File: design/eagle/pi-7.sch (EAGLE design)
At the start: 13 parts

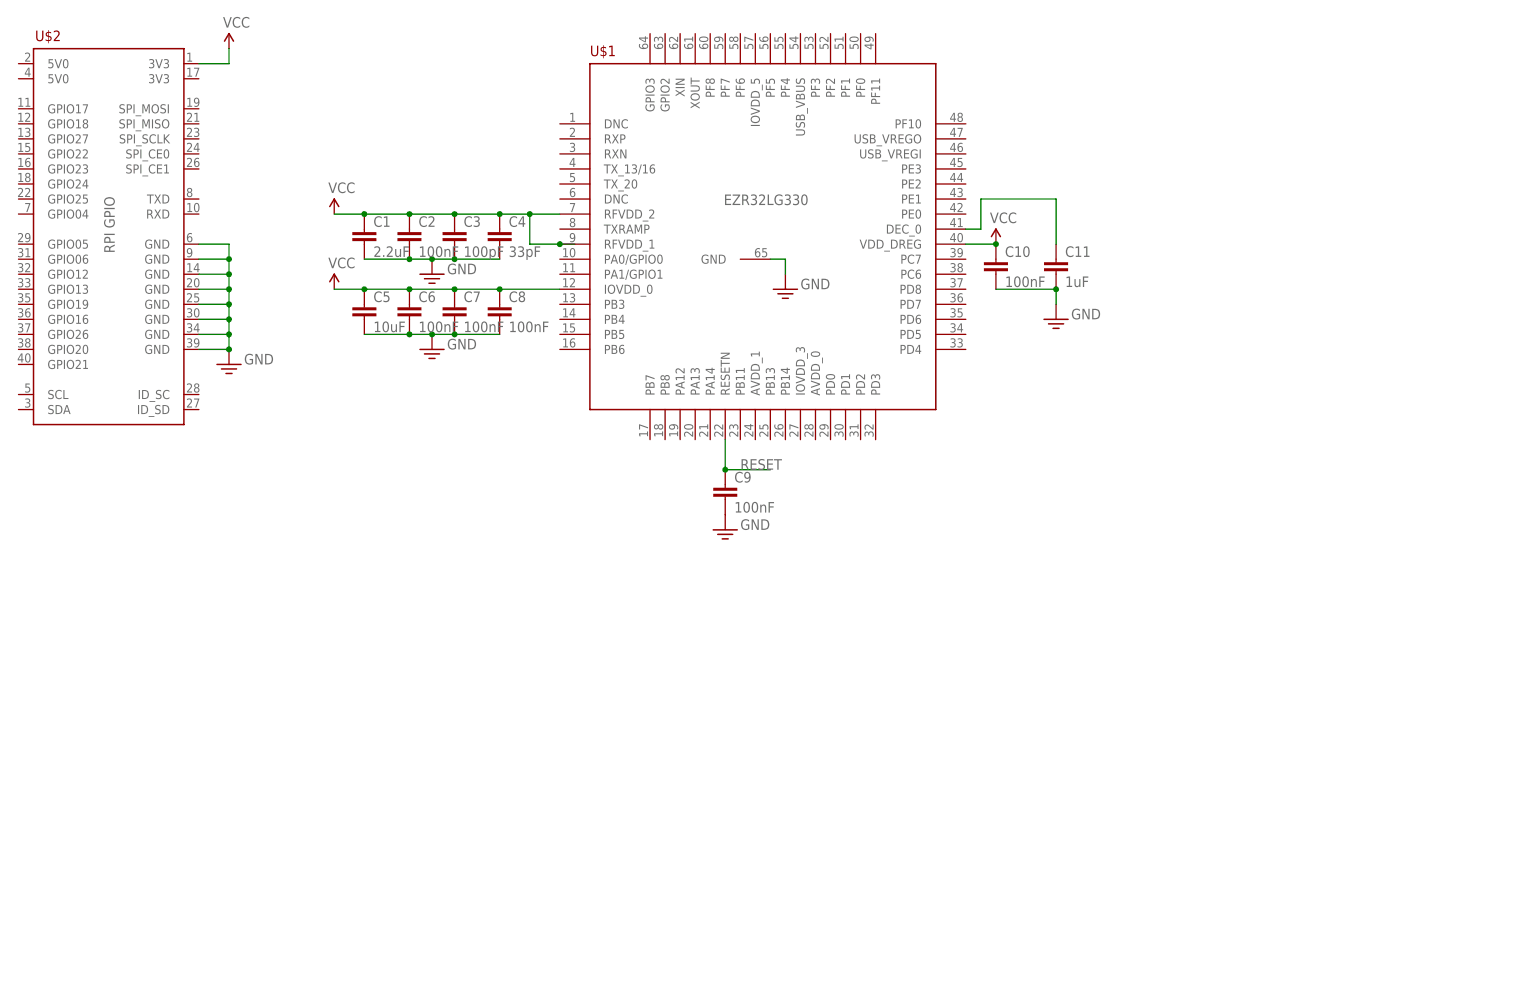
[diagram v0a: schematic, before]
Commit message: redesigned to match AN0016 + added JTAG (6pins)
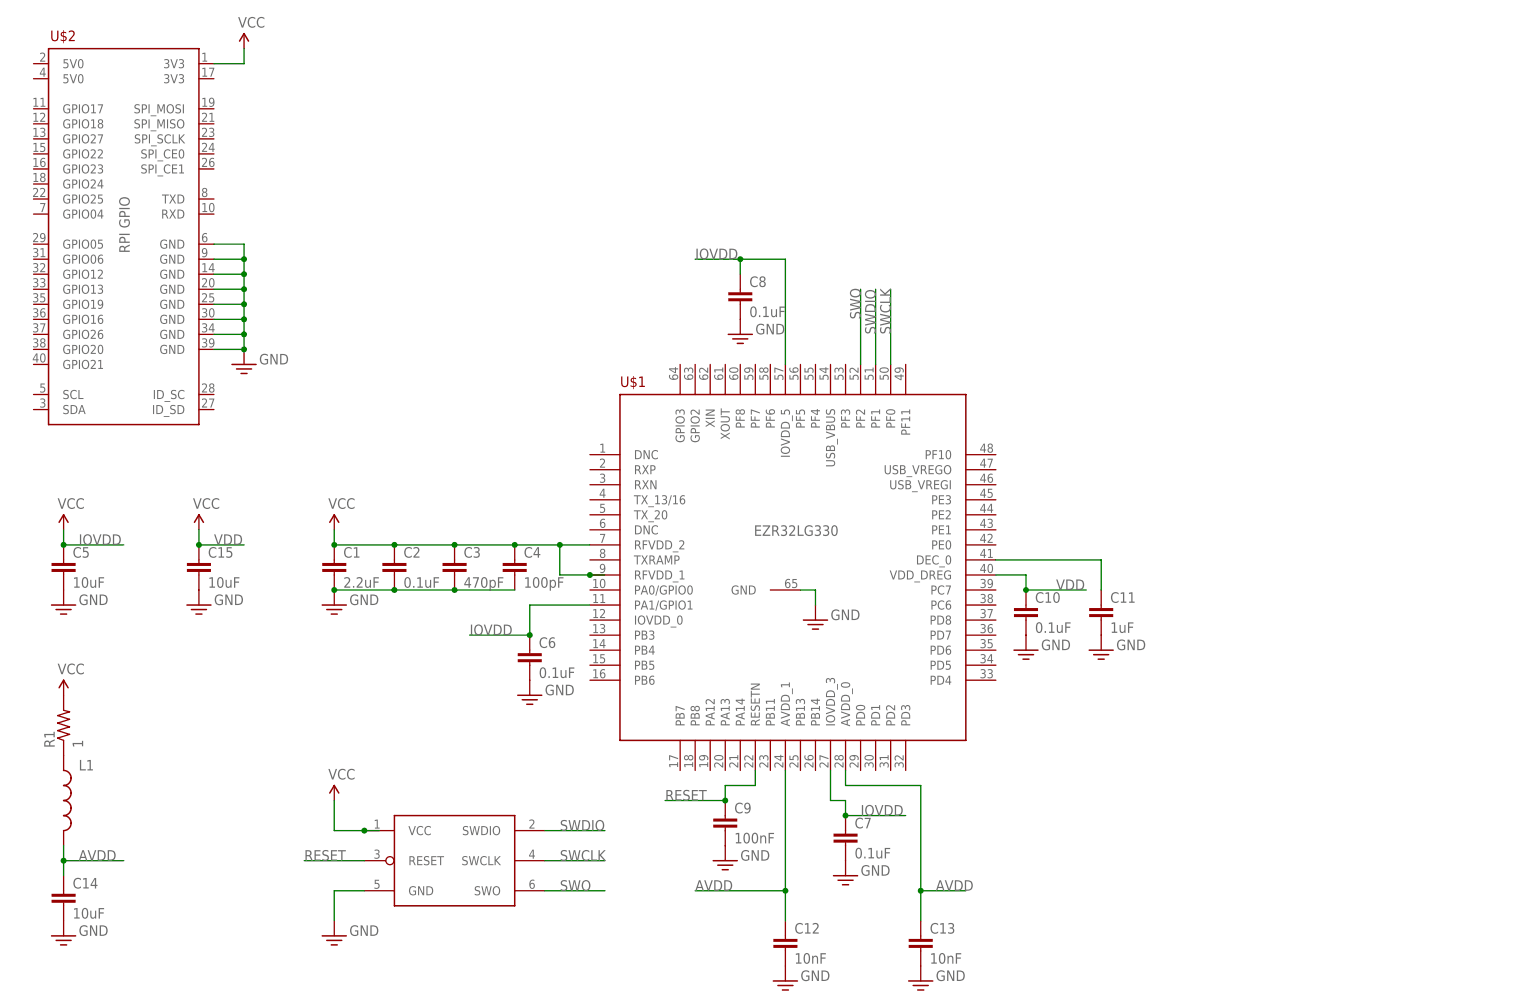
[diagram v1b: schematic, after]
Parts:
- added C12, C13: 10nF, passive:CAP0805
- added C14, C15: 10uF, passive:CAP0805
- added L1: (no value), passive:INDUCTOR0805
- added R1: 1, passive:RESISTOR0805-RES
- added U$3: JTAG-6PINS, setup:JTAG-6PINS
- C10, C2, C6, C7, C8: value 100nF -> 0.1uF
- C3: value 100pF -> 470pF
- C4: value 33pF -> 100pF
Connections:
- new net AVDD: C12.1, C13.1, C14.1, L1.2, U$1.AVDD_0, U$1.AVDD_1
- new net IOVDD: C5.1, C6.1, C7.1, C8.1, U$1.IOVDD_3, U$1.IOVDD_5, U$1.PA1/GPIO1
- new net N$4: L1.1, R1.1
- new net SWCLK: U$1.PF0, U$3.SWCLK
- new net SWDIO: U$1.PF1, U$3.SWDIO
- new net SWO: U$1.PF2, U$3.SWO
- new net VDD: C10.1, C15.1, U$1.VDD_DREG
- net GND-ISO: now also C12.2, C13.2, C14.2, C15.2, U$3.GND
- net RESET: now also U$3.RESET
- net VCC: now also R1.2, U$3.VCC; no longer C10.1, C5.1, C6.1, C7.1, C8.1, U$1.IOVDD_0, U$1.VDD_DREG
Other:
- moved on the sheet: C1, C10, C11, C2, C3, C4, C5, C6, C7, C8, C9, U$1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

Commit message: added crystals
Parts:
- added C16, C17: 10pF, passive:CAP0805
- added C18, C19: 22pF, passive:CAP0805
- added U$4: 26MHz, xtal:ABM8
- added U$5: 48MHz, xtal:ABM11
- added U$6: 32.768kHz, xtal:MS3V-T1R
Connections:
- new net HFXN: C17.1, U$1.PB14, U$5.3
- new net HFXP: C16.1, U$1.PB13, U$5.1
- new net LFXN: C19.1, U$1.PB8, U$6.2
- new net LFXP: C18.1, U$1.PB7, U$6.1
- new net XIN: U$1.XIN, U$4.1
- new net XOUT: U$1.XOUT, U$4.3
- net GND-ISO: now also C16.2, C17.2, C18.2, C19.2, U$4.GND@2, U$4.GND@4, U$5.GND@2, U$5.GND@4
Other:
- moved on the sheet: C12, C13, C7, C8, C9
